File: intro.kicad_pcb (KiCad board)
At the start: 2 copper layers, 148.5 x 110.1 mm, 122 parts, among them IC1 IS31FL3741A-QFLS4-TR, SW1 SW_Push, SW10 SW_Push, SW11 SW_Push, SW12 SW_Push, SW13 SW_Push, SW14 SW_Push, SW15 SW_Push, SW16 SW_Push, SW17 SW_Push, SW18 SW_Push, SW19 SW_Push, SW2 SW_Push, SW20 SW_Push, SW21 SW_Push, SW22 SW_Push, SW23 SW_Push, SW24 SW_Push, SW25 SW_Push, SW26 SW_Push, SW27 SW_Push, SW28 SW_Push, SW29 SW_Push, SW3 SW_Push, SW30 SW_Push, SW31 SW_Push, SW32 SW_Push, SW33 SW_Push, SW34 SW_Push, SW35 RotaryEncoder_Switch, SW4 SW_Push, SW5 SW_Push, SW6 SW_Push, SW7 SW_Push, SW8 SW_Push, SW9 SW_Push, U1 nice_nano

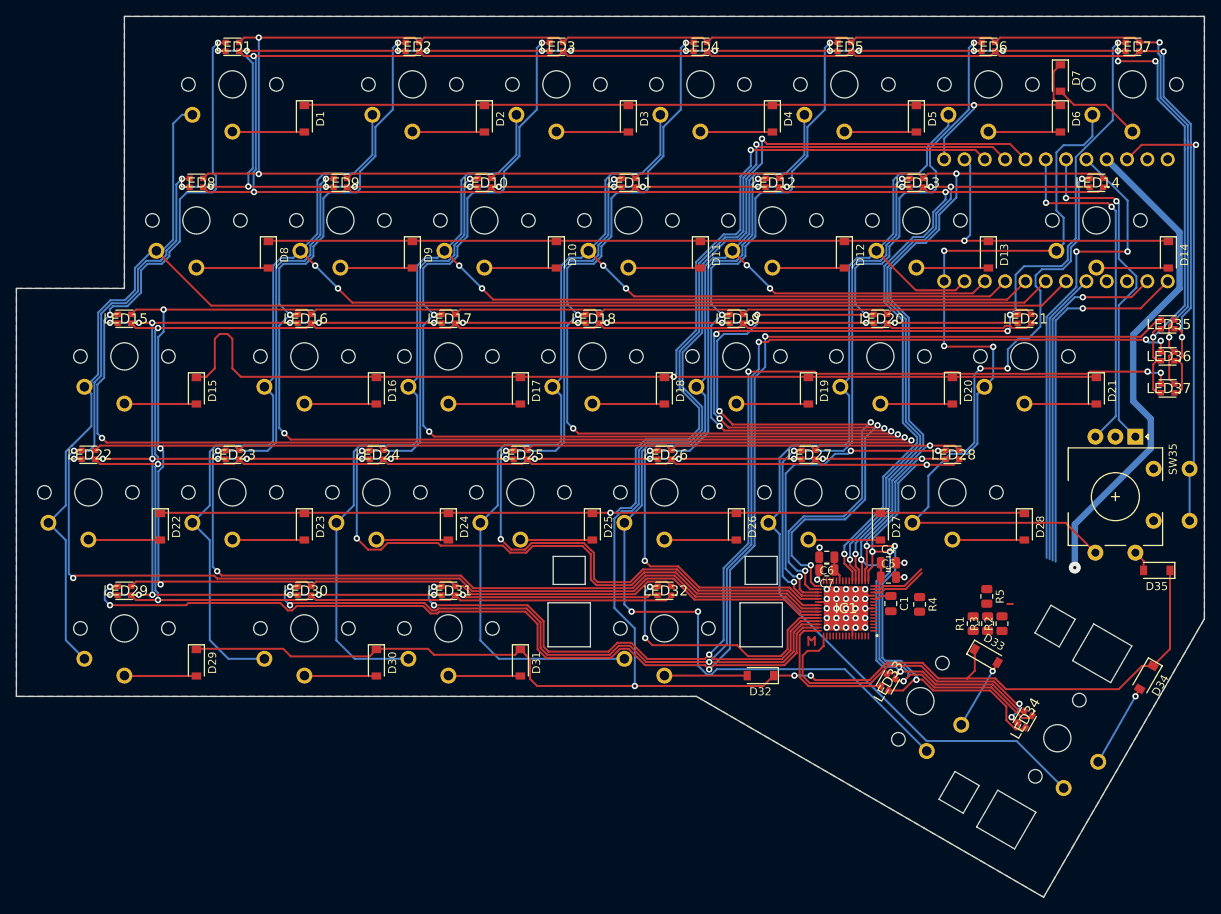
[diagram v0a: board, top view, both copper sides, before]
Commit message: remove traces and vias
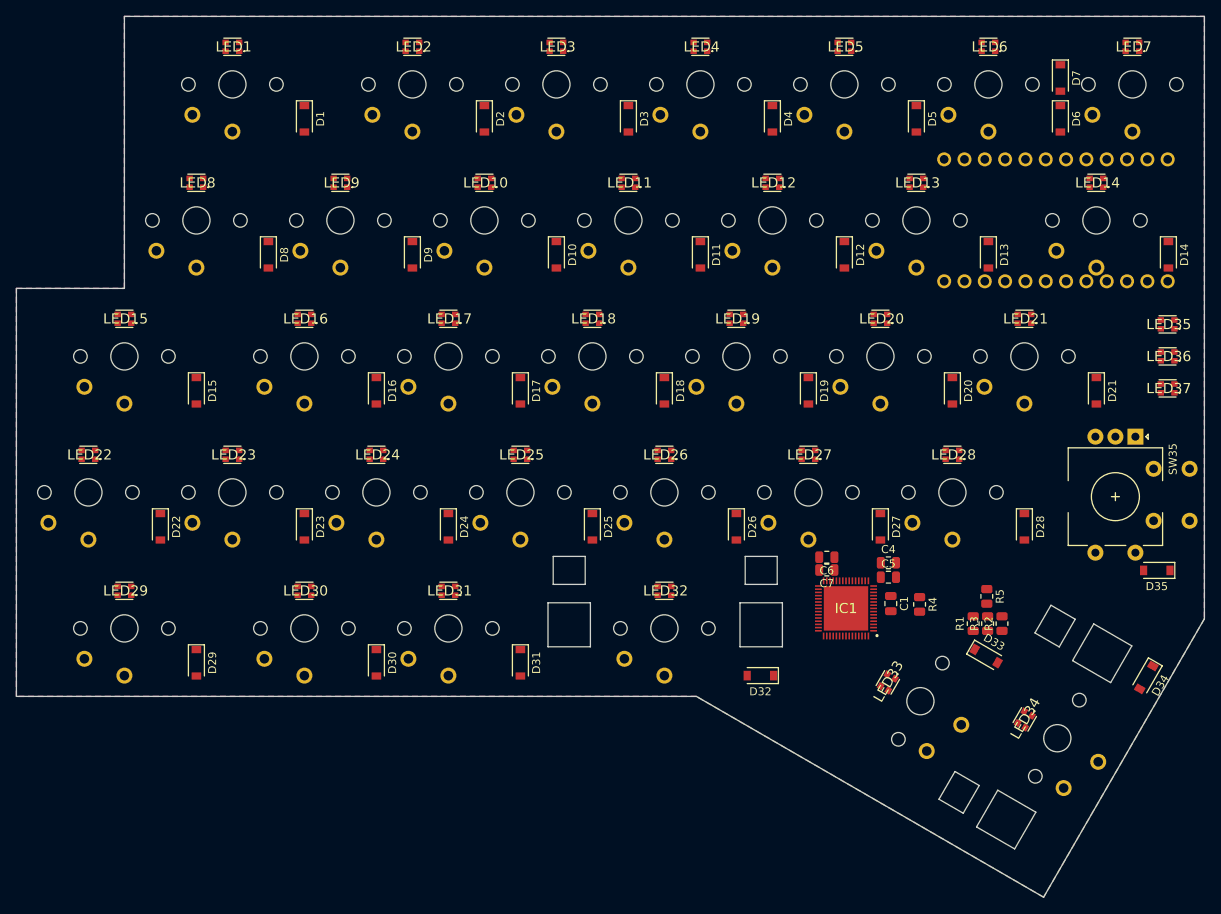
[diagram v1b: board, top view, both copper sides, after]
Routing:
- net RSW1: track 403.4 -> 0.00 mm, vias 37 -> 0
- net RSW2: track 390.5 -> 0.00 mm, vias 6 -> 0
- net RSW3: track 390.5 -> 0.00 mm, vias 7 -> 0
- net RSW4: track 368.8 -> 0.00 mm, vias 31 -> 0
- net RSW5: track 359.6 -> 0.00 mm, vias 6 -> 0
- net RSW6: track 357.5 -> 0.00 mm, vias 6 -> 0
- net row4: track 263.3 -> 0.00 mm, vias 4 -> 0
- net row3: track 201.2 -> 0.00 mm, vias 2 -> 0
- net col0: track 198.9 -> 0.00 mm
- net CS15: track 197.8 -> 0.00 mm, vias 4 -> 0
- net col1: track 188.5 -> 0.00 mm, vias 2 -> 0
- net row2: track 184.7 -> 0.00 mm, vias 2 -> 0
- net CS16: track 174.0 -> 0.00 mm, vias 6 -> 0
- net col2: track 168.9 -> 0.00 mm, vias 2 -> 0
- net CS1: track 163.7 -> 0.00 mm, vias 4 -> 0
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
